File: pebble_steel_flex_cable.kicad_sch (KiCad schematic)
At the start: 20 parts, among them J1 505551-1620, SW1 Select, SW2 DOWN, SW3 UP, SW4 BACK, U1 IS31FL3199-QFLS2-TR

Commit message: most of its mapped out
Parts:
- added C5, C6, C7, C8, C9: C, symbol Device:C
- added D10: CLV1L-FKB, LED_SMD:LED_Cree-PLCC4_3.2x2.8mm_CCW, symbol LED:CLV1L-FKB
- added D6, D7, D8: LED, symbol Device:LED
- added R6, R7: R, symbol Device:R
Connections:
- net GND: now also U1.16 (AD), C5.2, C6.1, R6.2
- net +3.3V: now reaches J1.11
- net +3.3V: now also J1.9, U1.1 (VCC), C5.1, C6.2, C7.1, C8.2, C9.2, D10.1 (A), D6.2 (A), D7.2 (A), D8.2 (A), R6.1, R7.1
- net at J1.5: now also R1.2
- net at U1.15 (R_EXT): now also R7.2
- net at U1.17 (IN): now also C7.2
- net at U1.2 (C_FILT): now also C9.1
- net at U1.20 (CLK/V_BM): now also C8.1
- net LED1: now reaches U1.3 (OUT1)
- net LED1: now also D8.1 (K)
- net LED2: now reaches U1.4 (OUT2)
- net LED2: now also D7.1 (K)
- net LED3: now reaches U1.5 (OUT3)
- net LED3: now also D6.1 (K)
- net LED_R: now reaches U1.6 (OUT4)
- net LED_R: now also D10.2 (RK)
- net LED_B: now reaches U1.8 (OUT5)
- net LED_B: now also D10.4 (BK)
- net LED_G: now reaches U1.9 (OUT6)
- net LED_G: now also D10.3 (GK)
- no-connect marks 0 -> 4
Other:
- moved on the sheet: U1

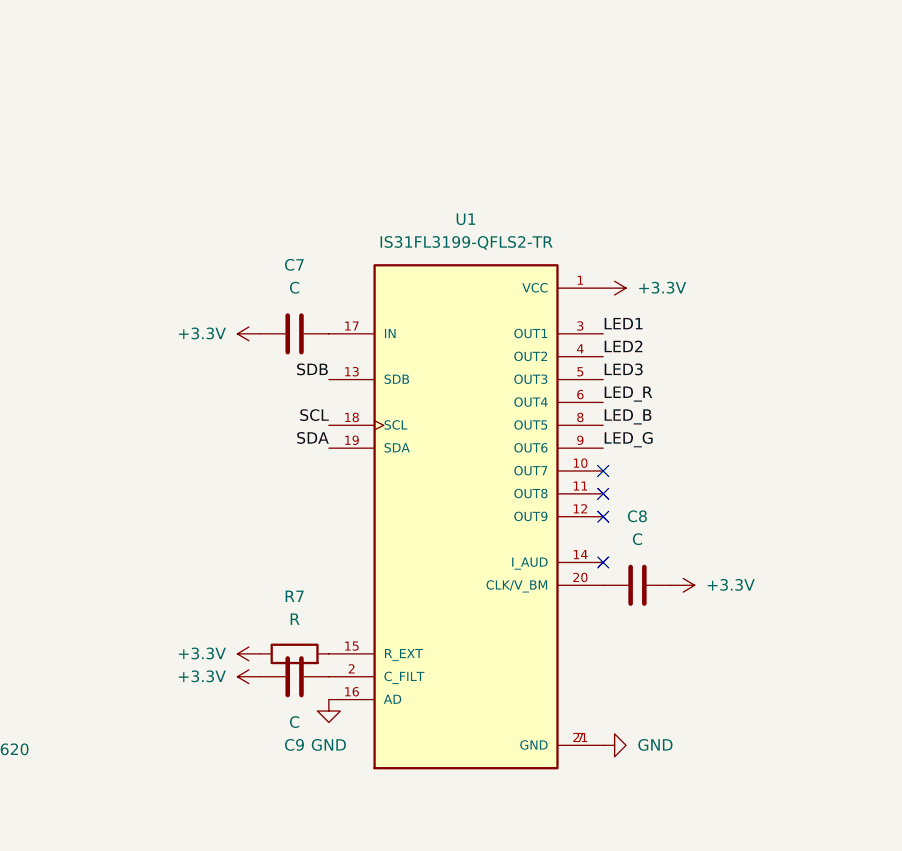
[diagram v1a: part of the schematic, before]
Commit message: fixed the layout and added the doc for the part
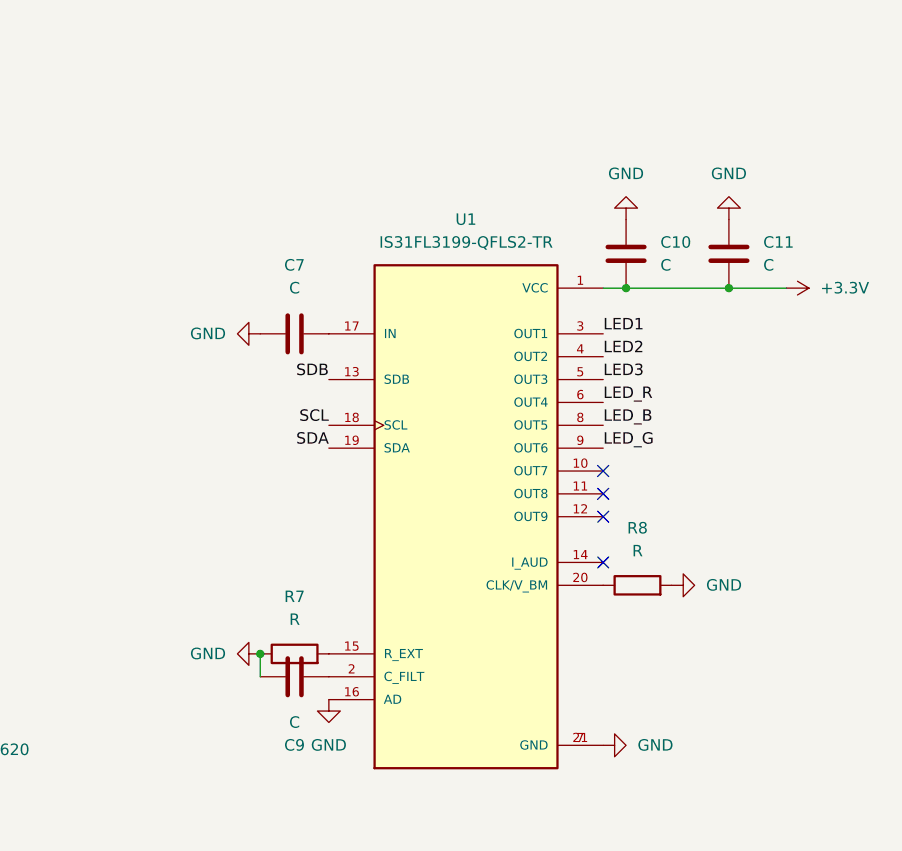
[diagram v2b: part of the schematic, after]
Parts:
- removed C8: C, symbol Device:C
- added C10, C11: C, symbol Device:C
- added R8: R, symbol Device:R
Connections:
- net +3.3V: now also C10.1, C11.1; no longer C7.1, C9.2, R7.1
- net GND: now also C7.1, C9.2, R7.1, C10.2, C11.2, R8.2
- net at U1.20 (CLK/V_BM): now also R8.1

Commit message: started layout
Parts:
- C1, C10, C11, C2, C3, C4, C5, C6, C7, C9: footprint (none) -> Capacitor_SMD:C_0201_0603Metric
- D10: value CLV1L-FKB -> Indicator LED; footprint LED_SMD:LED_Cree-PLCC4_3.2x2.8mm_CCW -> footprints:led_SML-LX0404SIUPGUSB
- D6, D7, D8: footprint (none) -> footprints:led_SML-LX0404SIUPGUSB
- J1: footprint 505551-1620:MOLEX_505551-1620 -> molex:MOLEX_505551-1620
- R1, R2, R3, R4, R5, R6, R7, R8: footprint (none) -> Resistor_SMD:R_0201_0603Metric
- SW1, SW2, SW3, SW4: footprint (none) -> button-TL3315NF250Q:SW_TL3315NF250Q
- U1: footprint IS31FL3199-QFLS2-TR:QFN40P300X300X80-21N -> chip:QFN40P300X300X80-21N
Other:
- moved on the sheet: C9

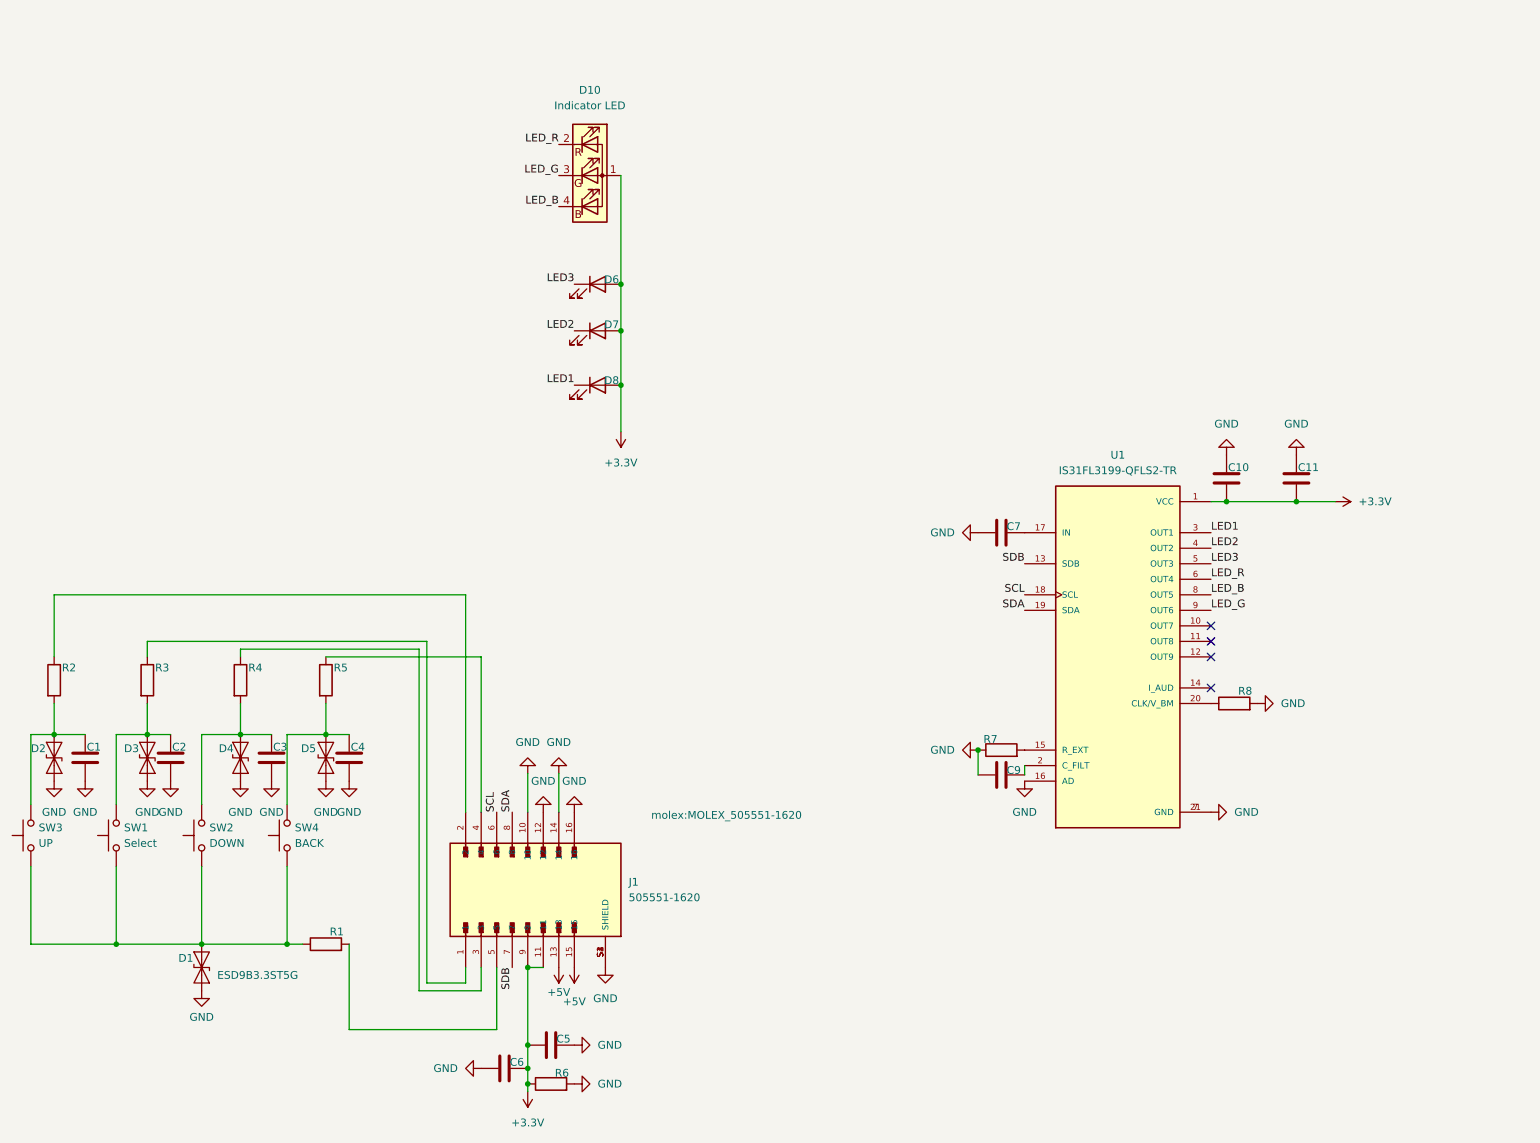
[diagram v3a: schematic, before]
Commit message: added the buttons and the battery connections
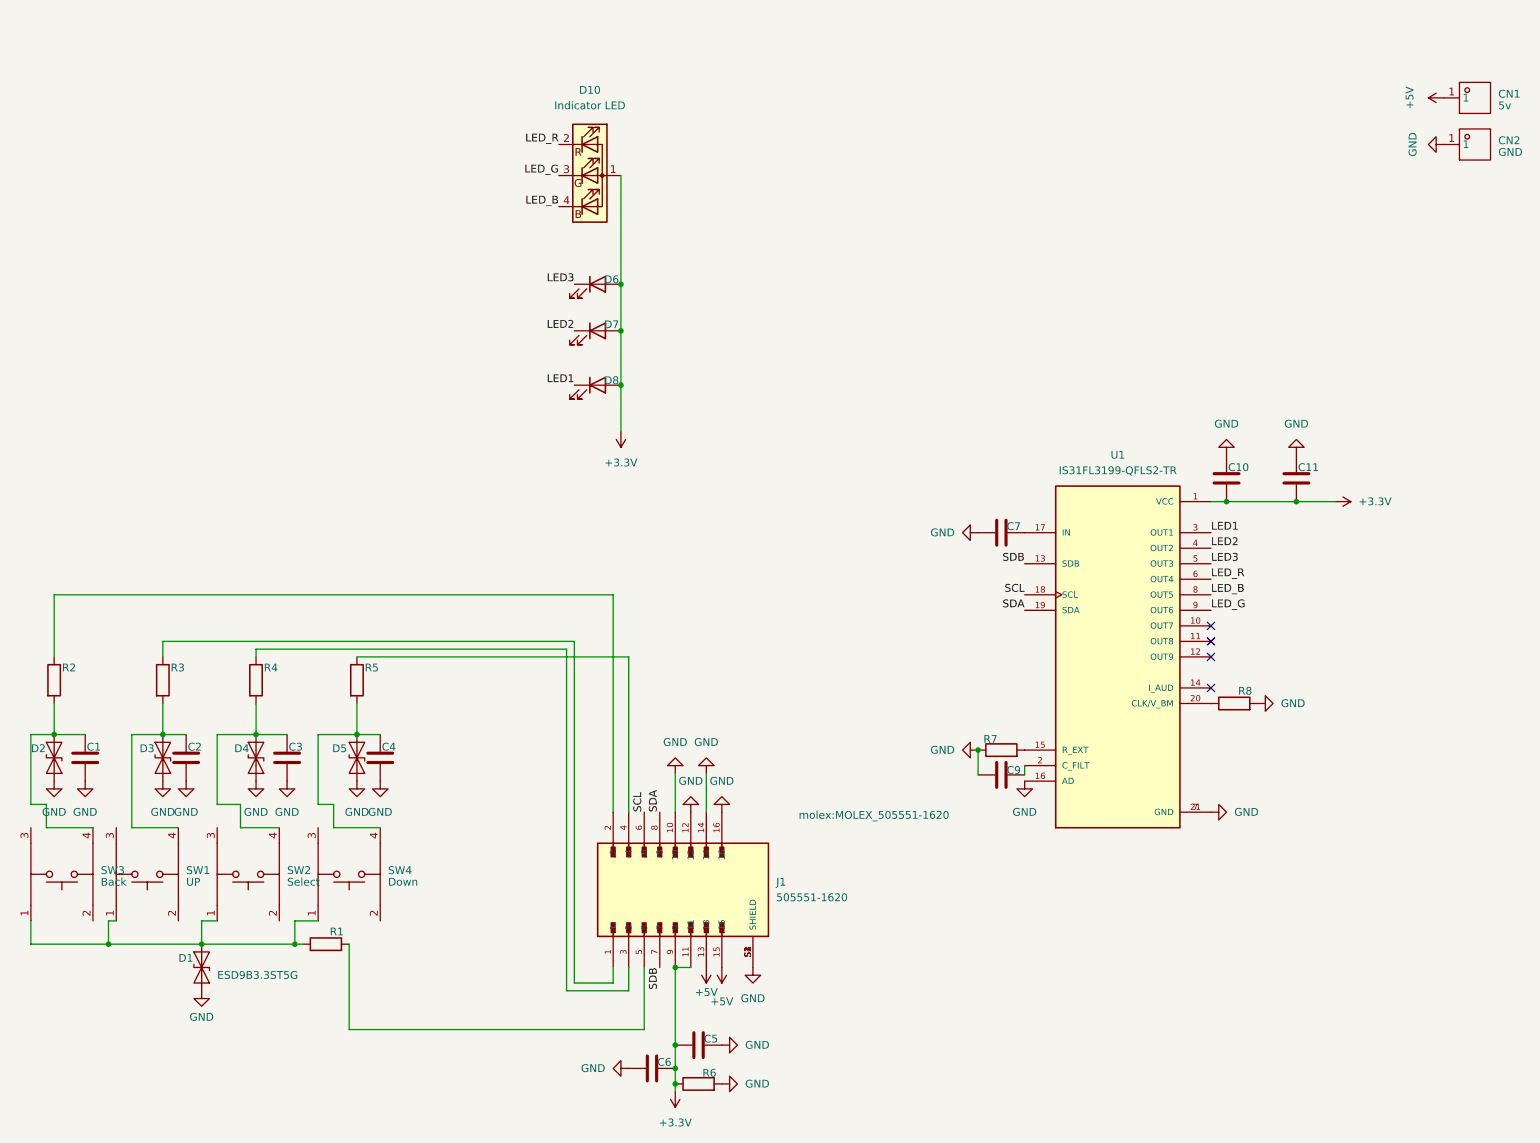
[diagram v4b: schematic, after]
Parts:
- removed SW1: Select, button-TL3315NF250Q:SW_TL3315NF250Q, symbol Switch:SW_Push
- removed SW2: DOWN, button-TL3315NF250Q:SW_TL3315NF250Q, symbol Switch:SW_Push
- removed SW3: UP, button-TL3315NF250Q:SW_TL3315NF250Q, symbol Switch:SW_Push
- removed SW4: BACK, button-TL3315NF250Q:SW_TL3315NF250Q, symbol Switch:SW_Push
- added CN1: 5v, S7121-42R:SMD_L2.7-W1.5, symbol S7121-42R:S7121-42R
- added CN2: GND, S7121-42R:SMD_L2.7-W1.5, symbol S7121-42R:S7121-42R
- added SW1: UP, SKSHAAE010:SW-SMD_SKSHAAE010, symbol SKSHAAE010:SKSHAAE010
- added SW2: Select, SKSHAAE010:SW-SMD_SKSHAAE010, symbol SKSHAAE010:SKSHAAE010
- added SW3: Back, SKSHAAE010:SW-SMD_SKSHAAE010, symbol SKSHAAE010:SKSHAAE010
- added SW4: Down, SKSHAAE010:SW-SMD_SKSHAAE010, symbol SKSHAAE010:SKSHAAE010
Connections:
- net +5V: now also CN1.1
- net GND: now also CN2.1
- net at C2.1, D3.2 (A2), R3.2: now also SW1.4
- net at C1.1, D2.2 (A2), R2.2: now also SW3.4
- net at D1.2 (A2), R1.1: now also SW1.1, SW2.1, SW3.1, SW4.1
- net at C4.1, D5.2 (A2), R5.2: now also SW4.4
- net at C3.1, D4.2 (A2), R4.2: now also SW2.4
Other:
- moved on the sheet: C2, C3, C4, C5, C6, D3, D4, D5, J1, R3, R4, R5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

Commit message: added the LED part
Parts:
- D6, D7, D8: footprint footprints:led_SML-LX0404SIUPGUSB -> LTW-020ZDCG:LTW-020ZDCG
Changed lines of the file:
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@@
 			)
 		)
-		(property "Footprint" "footprints:led_SML-LX0404SIUPGUSB"
+		(property "Footprint" "LTW-020ZDCG:LTW-020ZDCG"
 			(at 113.03 58.42 0)
 			(effects
@@
 			)
 		)
-		(property "Footprint" "footprints:led_SML-LX0404SIUPGUSB"
+		(property "Footprint" "LTW-020ZDCG:LTW-020ZDCG"
 			(at 113.03 74.93 0)
 			(effects
@@
 			)
 		)
-		(property "Footprint" "footprints:led_SML-LX0404SIUPGUSB"
+		(property "Footprint" "LTW-020ZDCG:LTW-020ZDCG"
 			(at 113.03 66.04 0)
 			(effects

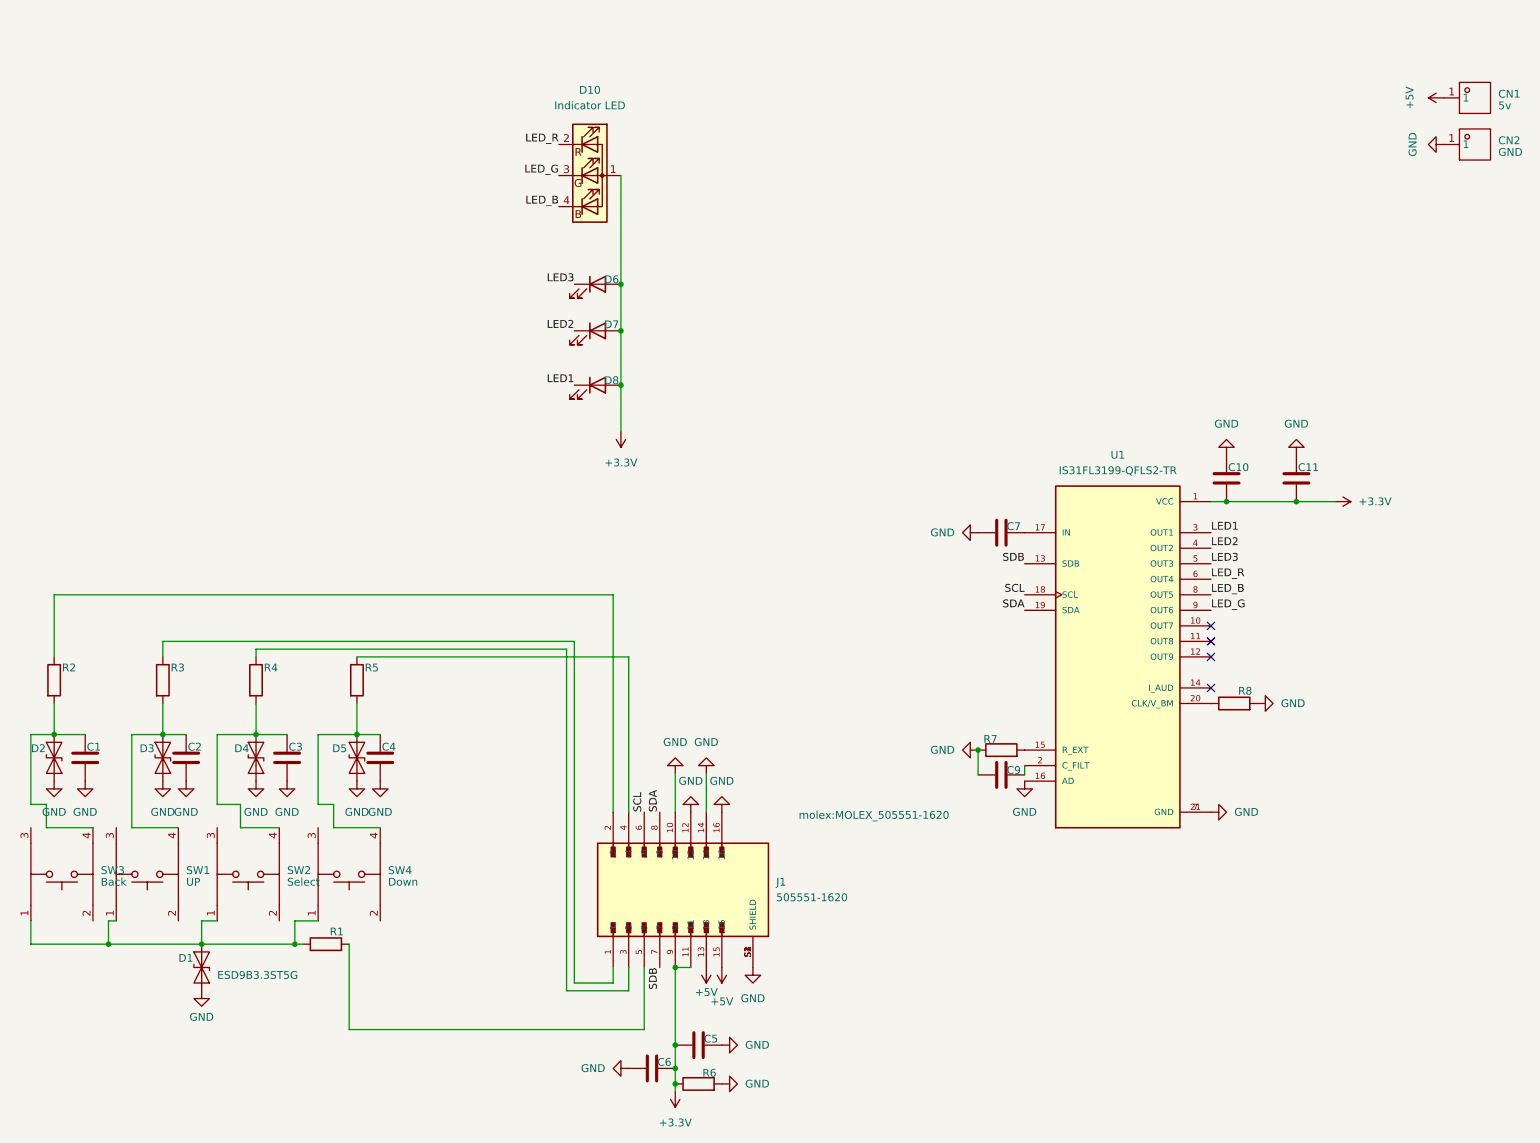
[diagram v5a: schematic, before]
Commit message: got the flex layed out
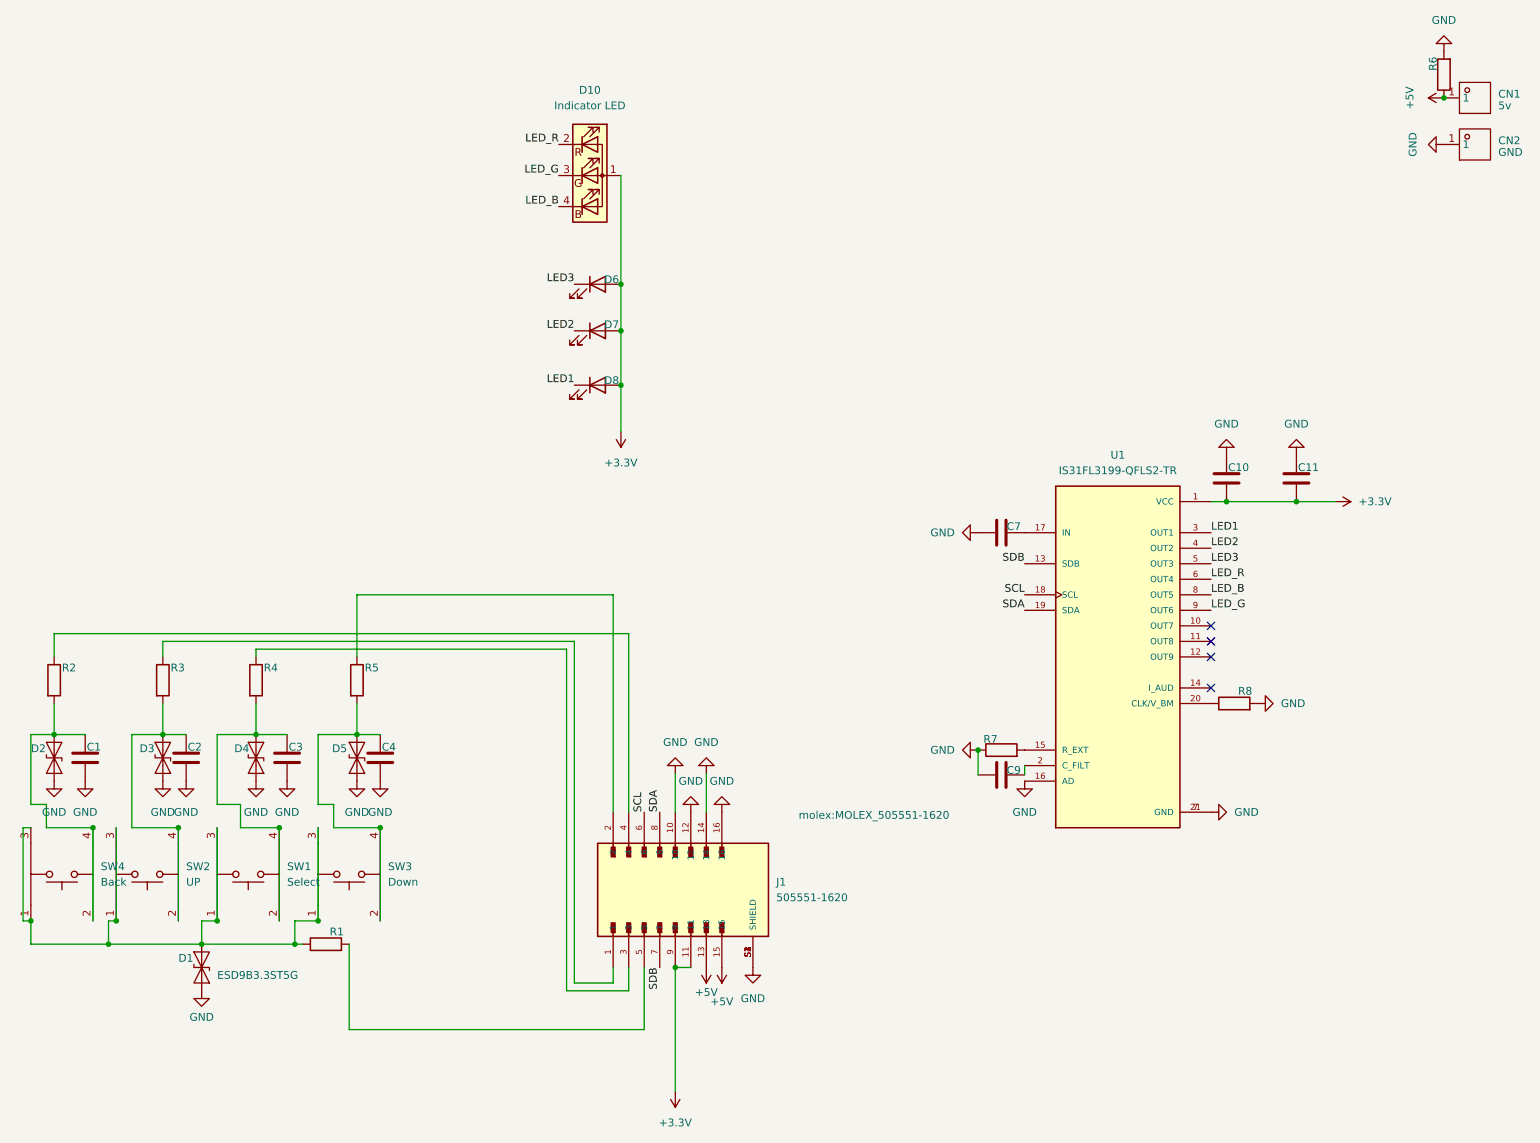
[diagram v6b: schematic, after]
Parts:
- removed C5, C6: C, Capacitor_SMD:C_0201_0603Metric, symbol Device:C
- renumbered SW2 to SW1, SW1 to SW2, SW4 to SW3, SW3 to SW4
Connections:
- net +3.3V: no longer R6.1
- net +5V: now also R6.1
- net at C2.1, D3.2 (A2), R3.2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: now also SW2.2
- net at C1.1, D2.2 (A2), R2.2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: now also SW4.2
- net at R2.1: now also J1.4; no longer J1.2
- net at R5.1: now also J1.2; no longer J1.4
- net at C4.1, D5.2 (A2), R5.2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: now also SW3.2
- net at C3.1, D4.2 (A2), R4.2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: now also SW1.2
- net at D1.2 (A2), R1.1, SW1.1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: now also SW1.3, SW2.3, SW3.3, SW4.3
